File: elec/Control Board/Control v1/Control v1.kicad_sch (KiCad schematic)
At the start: 2 parts, among them J1 Conn_02x12_Odd_Even

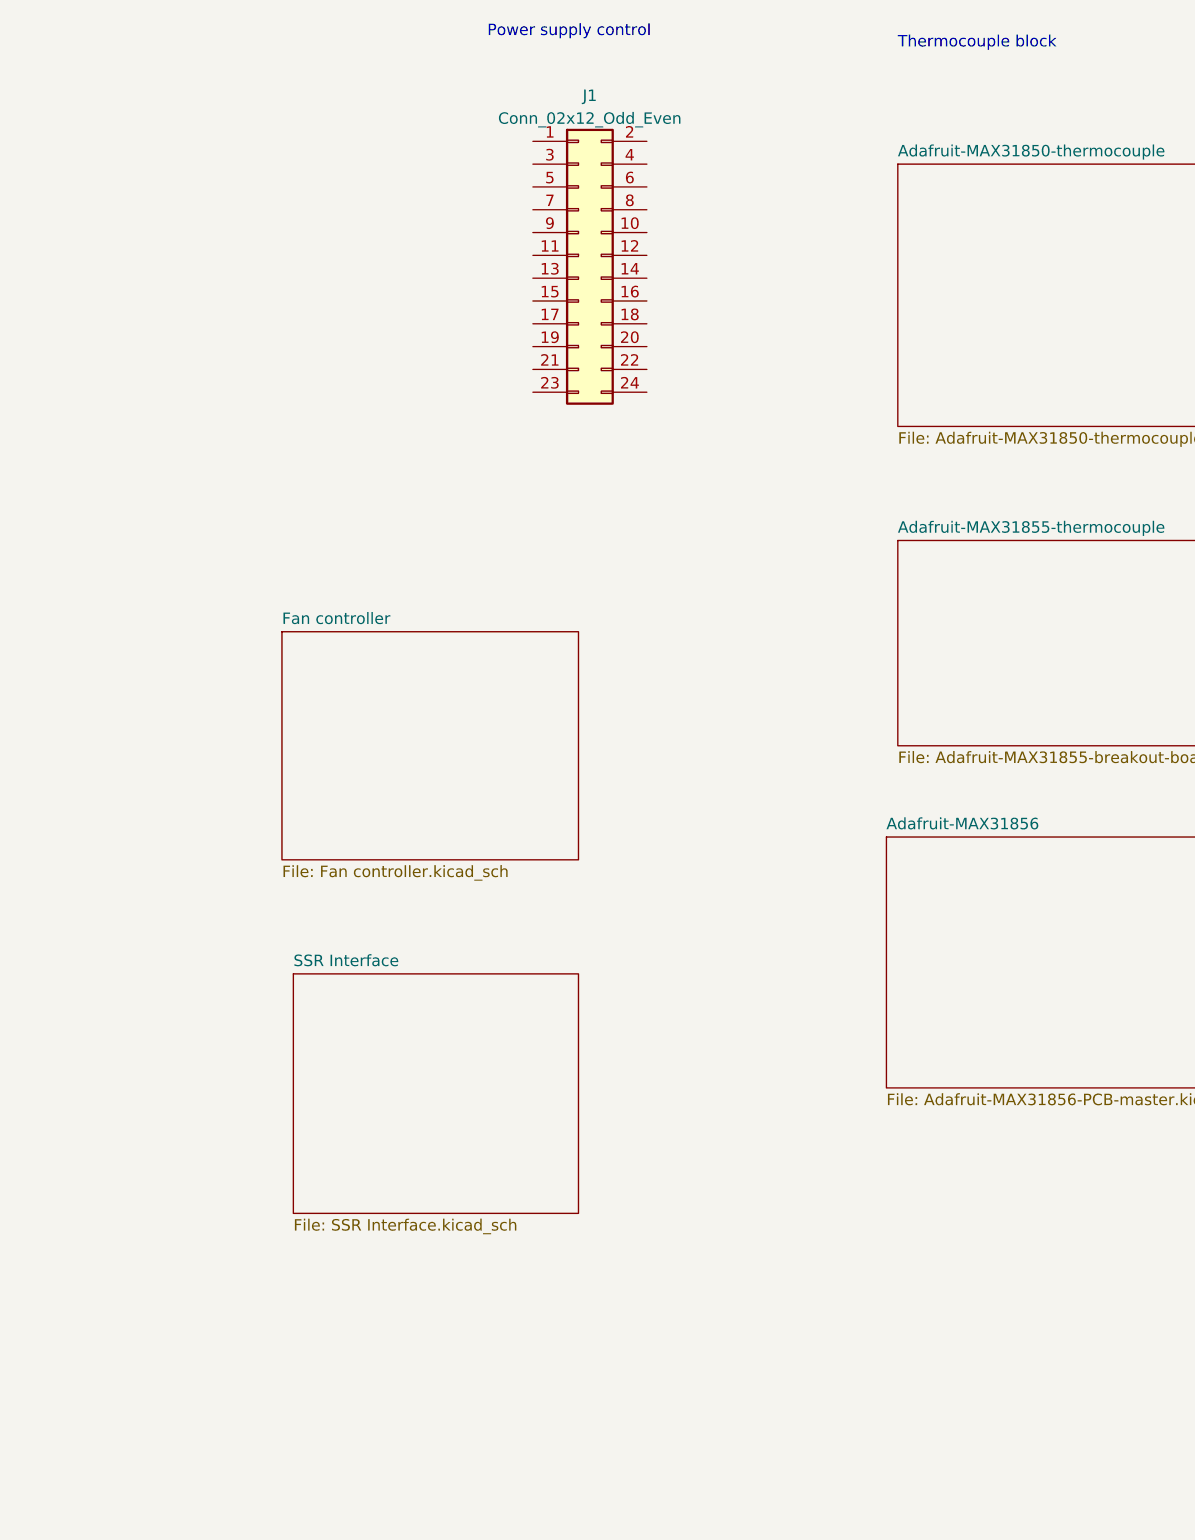
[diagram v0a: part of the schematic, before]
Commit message: added labels for heiarchy sheets, and first pass on basic control interface circuits
Signed-off-by: lokimetasmith <lokimail@gmail.com>
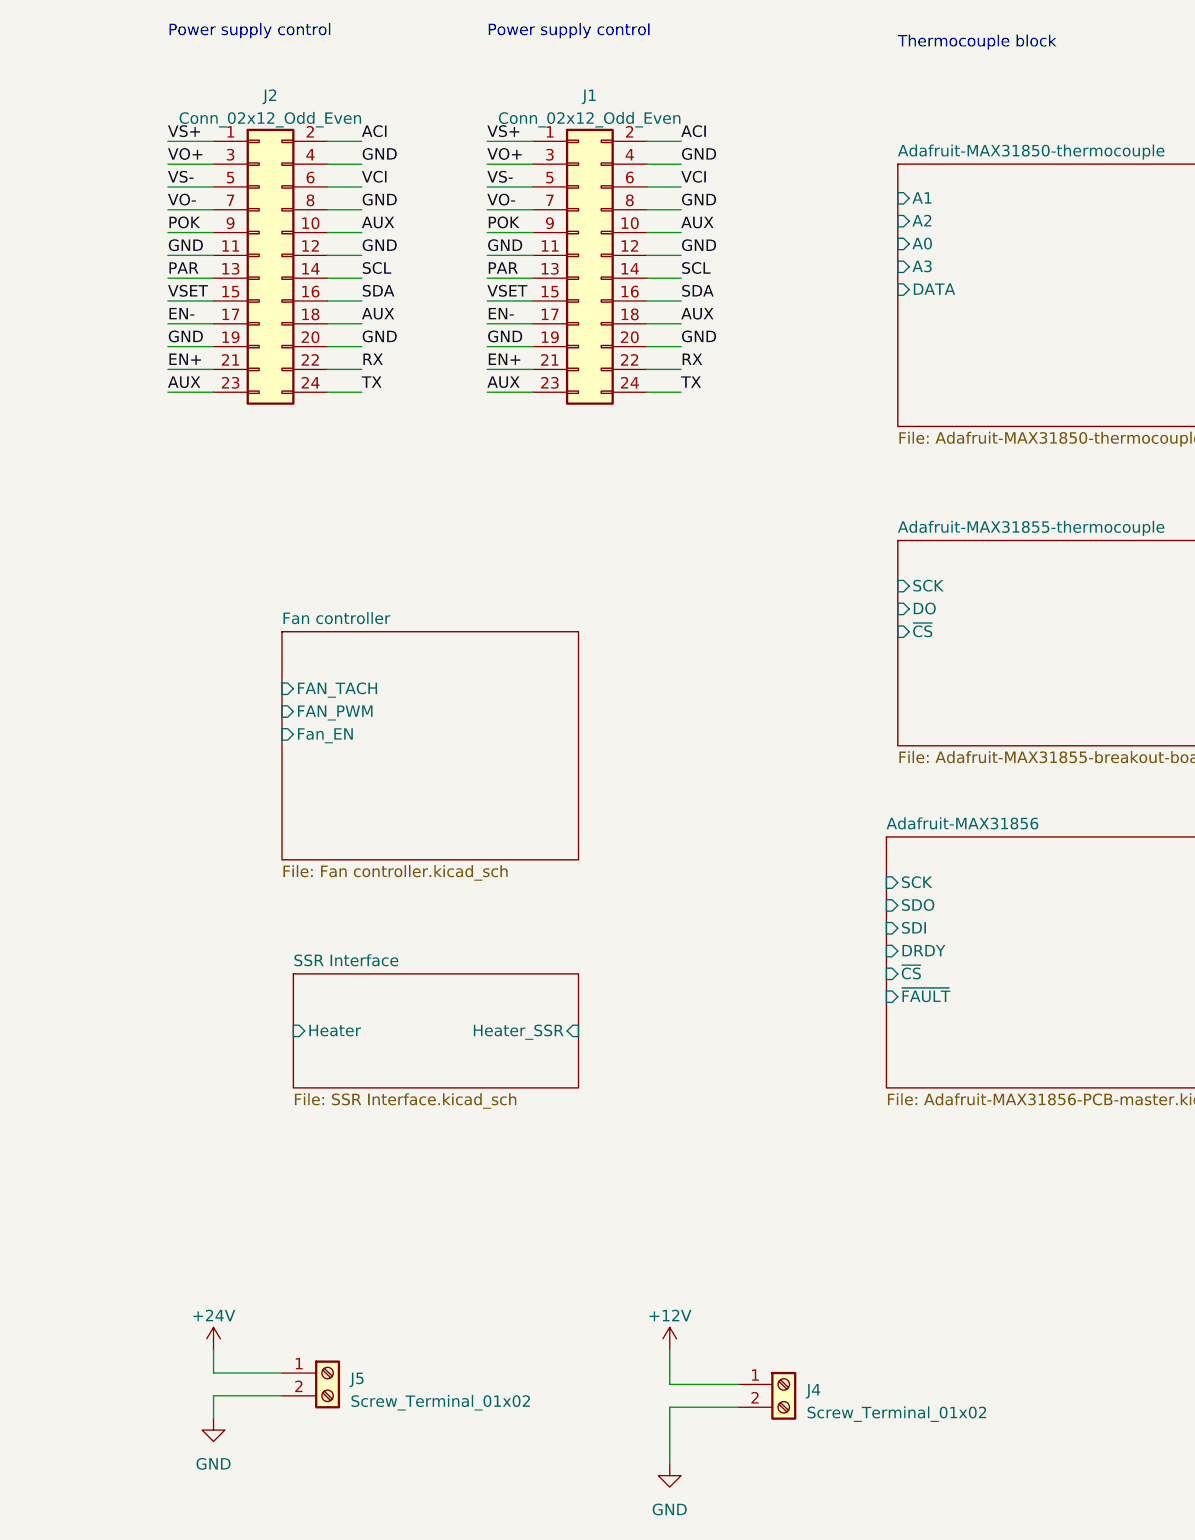
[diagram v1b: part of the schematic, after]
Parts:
- added J2: Conn_02x12_Odd_Even, Connector_PinHeader_2.00mm:PinHeader_2x12_P2.00mm_Vertical, symbol Connector_Generic:Conn_02x12_Odd_Even
- added J4, J5: Screw_Terminal_01x02, symbol Connector:Screw_Terminal_01x02
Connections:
- net VS+: now reaches J1.1 (Pin_1)
- net VS+: now also J2.1 (Pin_1)
- net AUX: now reaches J1.10 (Pin_10)
- net AUX: now also J1.18 (Pin_18), J1.23 (Pin_23), J2.10 (Pin_10), J2.18 (Pin_18), J2.23 (Pin_23)
- net GND: now reaches J1.11 (Pin_11)
- net GND: now also J1.12 (Pin_12), J1.19 (Pin_19), J1.20 (Pin_20), J1.4 (Pin_4), J1.8 (Pin_8), J2.11 (Pin_11), J2.12 (Pin_12), J2.19 (Pin_19), J2.20 (Pin_20), J2.4 (Pin_4), J2.8 (Pin_8), J4.2 (Pin_2), J5.2 (Pin_2)
- net PAR: now reaches J1.13 (Pin_13)
- net PAR: now also J2.13 (Pin_13)
- net SCL: now reaches J1.14 (Pin_14)
- net SCL: now also J2.14 (Pin_14)
- net VSET: now reaches J1.15 (Pin_15)
- net VSET: now also J2.15 (Pin_15)
- net SDA: now reaches J1.16 (Pin_16)
- net SDA: now also J2.16 (Pin_16)
- net EN-: now reaches J1.17 (Pin_17)
- net EN-: now also J2.17 (Pin_17)
- net ACI: now reaches J1.2 (Pin_2)
- net ACI: now also J2.2 (Pin_2)
- net EN+: now reaches J1.21 (Pin_21)
- net EN+: now also J2.21 (Pin_21)
- net RX: now reaches J1.22 (Pin_22)
- net RX: now also J2.22 (Pin_22)
- net TX: now reaches J1.24 (Pin_24)
- net TX: now also J2.24 (Pin_24)
- net VO+: now reaches J1.3 (Pin_3)
- net VO+: now also J2.3 (Pin_3)
- net VS-: now reaches J1.5 (Pin_5)
- net VS-: now also J2.5 (Pin_5)
- net VCI: now reaches J1.6 (Pin_6)
- net VCI: now also J2.6 (Pin_6)
- net VO-: now reaches J1.7 (Pin_7)
- net VO-: now also J2.7 (Pin_7)
- net POK: now reaches J1.9 (Pin_9)
- net POK: now also J2.9 (Pin_9)
- new net +12V: J4.1 (Pin_1)
- new net +24V: J5.1 (Pin_1)
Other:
- sheet Adafruit-MAX31850-thermocouple ports: added A0, A1, A2, A3, DATA; removed none
- sheet Adafruit-MAX31855-thermocouple ports: added DO, SCK, ~{CS}; removed none
- sheet Adafruit-MAX31856 ports: added DRDY, SCK, SDI, SDO, ~{CS}, ~{FAULT}; removed none
- sheet Fan controller ports: added FAN_PWM, FAN_TACH, Fan_EN; removed none
- sheet SSR Interface ports: added Heater, Heater_SSR; removed none

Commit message: imported Lee's changed inputs into the folder Control Board,
Also added in Robert's pin labels

ToDo: clean up broken links, and import in the layout files from Lee's project

Clean up the fan control pinout, the DB25 is a bit of a mess
consider using IDC to DB25 connectors for ease of assembly and installation.


Signed-off-by: lokimetasmith <lokimail@gmail.com>
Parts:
- removed J2: Conn_02x12_Odd_Even, Connector_PinHeader_2.00mm:PinHeader_2x12_P2.00mm_Vertical, symbol Connector_Generic:Conn_02x12_Odd_Even
- added H1, H2, H3, H4, H5: MountingHole_Pad_3.5mm, GeneralPurposeAlarmDevicePCB:MountingHole_3.5mm_Pad_Via, symbol GPAD_SCH_LIB:MountingHole_Pad_3.5mm
- added J14, J15, J17, J18: Conn_01x08, Connector_PinSocket_2.54mm:PinSocket_1x08_P2.54mm_Vertical, symbol Connector_Generic:Conn_01x08
- added J16: Conn_01x08, Connector_PinHeader_2.54mm:PinHeader_1x08_P2.54mm_Vertical, symbol Connector_Generic:Conn_01x08
- added J19: Conn_02x18_Odd_Even, Connector_PinSocket_2.54mm:PinSocket_2x18_P2.54mm_Vertical, symbol Connector_Generic:Conn_02x18_Odd_Even
- added J20: Conn_01x10_MountingPin, Connector_PinSocket_2.54mm:PinSocket_1x10_P2.54mm_Vertical, symbol Connector_Generic_MountingPin:Conn_01x10_MountingPin
- added J7: DB9_Female_MountingHoles, Connector_Dsub:DSUB-9_Female_Horizontal_P2.77x2.84mm_EdgePinOffset4.94mm_Housed_MountingHolesOffset7.48mm, symbol Connector:DB9_Female_MountingHoles
- added MF1: PCB_PolyVent_SPI_Controller_VER1, NA, symbol GPAD_SCH_LIB:PCB_GPAD_VER1
- added SW1: SW_DIP_x08, PubInv_PCB:SMDIP-16_L11.39_W6.7mm, symbol Switch:SW_DIP_x08
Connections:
- net RX is gone; now on net AUX: J1.22 (Pin_22)
- net TX is gone; now on net D_PSU_TX: J1.24 (Pin_24)
- net ACI: now also J1.14 (Pin_14); no longer J1.2 (Pin_2)
- net AUX: now also J1.11 (Pin_11); no longer J1.10 (Pin_10), J1.23 (Pin_23)
- net EN+: now also J1.12 (Pin_12); no longer J1.21 (Pin_21)
- net EN-: now also J1.10 (Pin_10); no longer J1.17 (Pin_17)
- net GND: now also A1.GND1 (GND), A1.GND2 (GND), A1.GND3 (GND), A1.GND5 (GND), A1.GND6 (GND), J1.13 (Pin_13), J1.15 (Pin_15), J1.17 (Pin_17), J1.21 (Pin_21), J1.5 (Pin_5), J1.9 (Pin_9), H1.1, H2.1, H3.1, H4.1, H5.1, J16.2 (Pin_2), J16.3 (Pin_3), J19.35 (Pin_35), J19.36 (Pin_36), J20.4 (Pin_4), J7.0 (PAD), J7.3, J7.6, J7.7, J7.8, J7.9; no longer J1.11 (Pin_11), J1.12 (Pin_12), J1.19 (Pin_19), J1.20 (Pin_20), J1.4 (Pin_4), J1.8 (Pin_8)
- net PAR: now also J1.8 (Pin_8); no longer J1.13 (Pin_13)
- net POK: now also J1.6 (Pin_6); no longer J1.9 (Pin_9)
- net SCL: now also A1.D21 (D21/SCL), J1.20 (Pin_20); no longer J1.14 (Pin_14)
- net SDA: now also A1.D20 (D20/SDA), J1.19 (Pin_19); no longer J1.16 (Pin_16)
- net VCI: now also J1.16 (Pin_16); no longer J1.6 (Pin_6)
- net VO+: now also J1.1 (Pin_1); no longer J1.3 (Pin_3)
- net VO-: now also J1.3 (Pin_3); no longer J1.7 (Pin_7)
- net VS+: now also J1.2 (Pin_2); no longer J1.1 (Pin_1)
- net VS-: now also J1.4 (Pin_4); no longer J1.5 (Pin_5)
- net VSET: now also J1.7 (Pin_7); no longer J1.15 (Pin_15)
- net +3.3V: now reaches A1.3V3 (3.3V)
- net +3.3V: now also J16.5 (Pin_5)
- net +5V: now reaches A1.5V1 (5V)
- net +5V: now also J16.4 (Pin_4)
- net 5V3: now reaches A1.5V3 (5V)
- net 5V3: now also J19.1 (Pin_1)
- net 5V4: now reaches A1.5V4 (5V)
- net 5V4: now also J19.2 (Pin_2)
- net BLOWER_TACH: now reaches A1.A0
- net BLOWER_TACH: now also J17.1 (Pin_1)
- net at A1.A1: now also J17.2 (Pin_2)
- net at A1.A10: now also J15.3 (Pin_3)
- net at A1.A11: now also J15.4 (Pin_4)
- net at A1.A2: now also J17.3 (Pin_3)
- net at A1.A3: now also J17.4 (Pin_4)
- net at A1.A4: now also J17.5 (Pin_5)
- net at A1.A5: now also J17.6 (Pin_6)
- net at A1.A6: now also J17.7 (Pin_7)
- net at A1.A7: now also J17.8 (Pin_8)
- net at A1.A8: now also J15.1 (Pin_1)
- net at A1.A9: now also J15.2 (Pin_2)
- net AREF: now reaches A1.AREF
- net AREF: now also J20.3 (Pin_3)
- net CANR: now reaches A1.CANR (CANRX)
- net CANR: now also J15.7 (Pin_7)
- net CANT: now reaches A1.CANT (CANTX)
- net CANT: now also J15.8 (Pin_8)
- net D0: now reaches A1.D0 (D0/RX0)
- net D0: now also J18.1 (Pin_1)
- net D1: now reaches A1.D1 (D1/TX0)
- net D1: now also J18.2 (Pin_2)
- net at A1.D10 (D10_CS0): now also J20.8 (Pin_8)
- net at A1.D11: now also J20.7 (Pin_7)
- net at A1.D12: now also J20.6 (Pin_6)
- net at A1.D13: now also J20.5 (Pin_5)
- net at A1.D14 (D14/TX3): now also J14.1 (Pin_1)
- net at A1.D15 (D15/RX3): now also J14.2 (Pin_2)
- net at A1.D16 (D16/TX2): now also J14.3 (Pin_3)
- net at A1.D17 (D17/RX2): now also J14.4 (Pin_4)
- net D_PSU_TX: now reaches A1.D18 (D18/TX1)
- net D_PSU_TX: now also J14.5 (Pin_5)
- net D_PSU_RX: now reaches A1.D19 (D19/RX1)
- net D_PSU_RX: now also J1.23 (Pin_23), J14.6 (Pin_6)
- net at A1.D2: now also J18.3 (Pin_3)
- net at A1.D22: now also J19.3 (Pin_3)
- net D23: now reaches A1.D23
- net D23: now also J14.7 (Pin_7), J19.4 (Pin_4)
- net at A1.D24: now also J19.5 (Pin_5)
- net D25: now reaches A1.D25
- net D25: now also J19.6 (Pin_6)
- net at A1.D26: now also J19.7 (Pin_7)
- net D27: now reaches A1.D27
- net D27: now also J19.8 (Pin_8)
- net at A1.D28: now also J19.9 (Pin_9)
- net D29: now reaches A1.D29
- net D29: now also J19.10 (Pin_10)
- net at A1.D3: now also J18.4 (Pin_4)
- net at A1.D30: now also J19.11 (Pin_11)
- net D31: now reaches A1.D31
- net D31: now also J19.12 (Pin_12)
- net at A1.D32: now also J19.13 (Pin_13)
- net D33: now reaches A1.D33
- net D33: now also J19.14 (Pin_14)
- net at A1.D34: now also J19.15 (Pin_15)
- net D35: now reaches A1.D35
- net D35: now also J19.16 (Pin_16)
- net at A1.D36: now also J19.17 (Pin_17)
- net D37: now reaches A1.D37
- net D37: now also J19.18 (Pin_18)
- net at A1.D38: now also J19.19 (Pin_19)
- net D39: now reaches A1.D39
- net D39: now also J19.20 (Pin_20)
- net ONE_WIRE_TC: now reaches A1.D4 (D4_CS1)
- net ONE_WIRE_TC: now also J18.5 (Pin_5)
- net at A1.D40: now also J19.21 (Pin_21)
- net D41: now reaches A1.D41
- net D41: now also J19.22 (Pin_22)
- net at A1.D42: now also J19.23 (Pin_23)
- net D43: now reaches A1.D43
- net D43: now also J19.24 (Pin_24)
- net at A1.D44: now also J19.25 (Pin_25)
- net D45: now reaches A1.D45
- net D45: now also J19.26 (Pin_26)
- net at A1.D46: now also J19.27 (Pin_27)
- net D47: now reaches A1.D47
- net D47: now also J19.28 (Pin_28)
- net at A1.D48: now also J19.29 (Pin_29)
- net D49: now reaches A1.D49
- net D49: now also J19.30 (Pin_30)
- net at A1.D5: now also J18.6 (Pin_6)
- net at A1.D50: now also J19.31 (Pin_31)
- net D51: now reaches A1.D51
- net D51: now also J19.32 (Pin_32)
- net at A1.D52 (D52_CS2): now also J19.33 (Pin_33)
- net at A1.D53: now also J19.34 (Pin_34)
- net at A1.D6: now also J18.7 (Pin_7)
- net at A1.D7: now also J18.8 (Pin_8)
- net at A1.D8: now also J20.10 (Pin_10)
- net BLOWER_PWM: now reaches A1.D9
- net BLOWER_PWM: now also J20.9 (Pin_9)
- net DAC0: now reaches A1.DAC0
- net DAC0: now also J15.5 (Pin_5)
- net DAC1: now reaches A1.DAC1
- net DAC1: now also J15.6 (Pin_6)
- net at A1.IORF (IOREF): now also J16.7 (Pin_7)
- net CIPO: now reaches A1.MISO (SPI_MISO)
- net COPI: now reaches A1.MOSI (SPI_MOSI)
- net at A1.RST1 (RESET): now also J16.6 (Pin_6)
- net SPI_SCK: now reaches A1.SCK (SPI_SCK)
- net SCL1: now reaches A1.SCL1
- net SCL1: now also J20.1 (Pin_1)
- net SDA1: now reaches A1.SDA1
- net SDA1: now also J20.2 (Pin_2)
- net at A1.VIN: now also J16.1 (Pin_1)
- new net D22: J14.8 (Pin_8)
- new net I2C_LevelShift/SCL_5V: J7.2
- new net I2C_LevelShift/SDA_5V: J7.4
- new net SPI_ControllerLevel_Shifter/COPI_nCS: SW1.1, SW1.2, SW1.3, SW1.4, SW1.5, SW1.6, SW1.7, SW1.8
- new net nCS1_3V3: SW1.16
- new net nCS2_3V3: SW1.15
- new net nCS3_3V3: SW1.14
- new net nCS4_3V3: SW1.13
- new net nCS5_3V3: SW1.12
- new net nCS6_3V3: SW1.11
- new net nCS7_3V3: SW1.10
- new net nCS8_3V3: SW1.9
- no-connect marks 0 -> 1
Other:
- added sheet I2C_LevelShift (I2C_Level_Shifter.kicad_sch)
- added sheet SPI_ControllerLevel_Shifter (SPI_ControllerLevel_Shifter.kicad_sch)
- note added: "Due Pin Number Connection Notes A0 Blower Tachometer D4 Dallas One-Wire connection to Thermocouple Breakouts D9 Blower PWM D18 Digital Power Supply TF800 Pin 23 This is Serial1 TX https://assets.alliedelec.com/v1560852133/Datasheets/1d230174086e96b6e4801d1c963649f3.pdf D19 Digital Power Supply TF800 Pin 24 This is Serial1 RX https://assets.alliedelec.com/v1560852133/Datasheets/1d230174086e96b6e48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"
- note added: "| **Pin #** | **Function** | **Description** | **Pin #** | **Function** | **Description** | |----------- |-------------- |-------------------------------------- |----------- |-------------- |-------------------------------------- | | 1 | VS+ | Remote Sense (+) | 13 | ACI | I Program | | 2 | VO+ | Positive Output Voltage | 14 | GND | Ground | | 3 | VX- | Remote Sense (-) | 15 | VCI | V Program | |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"
- moved on the sheet: A1, J1, J4, J5

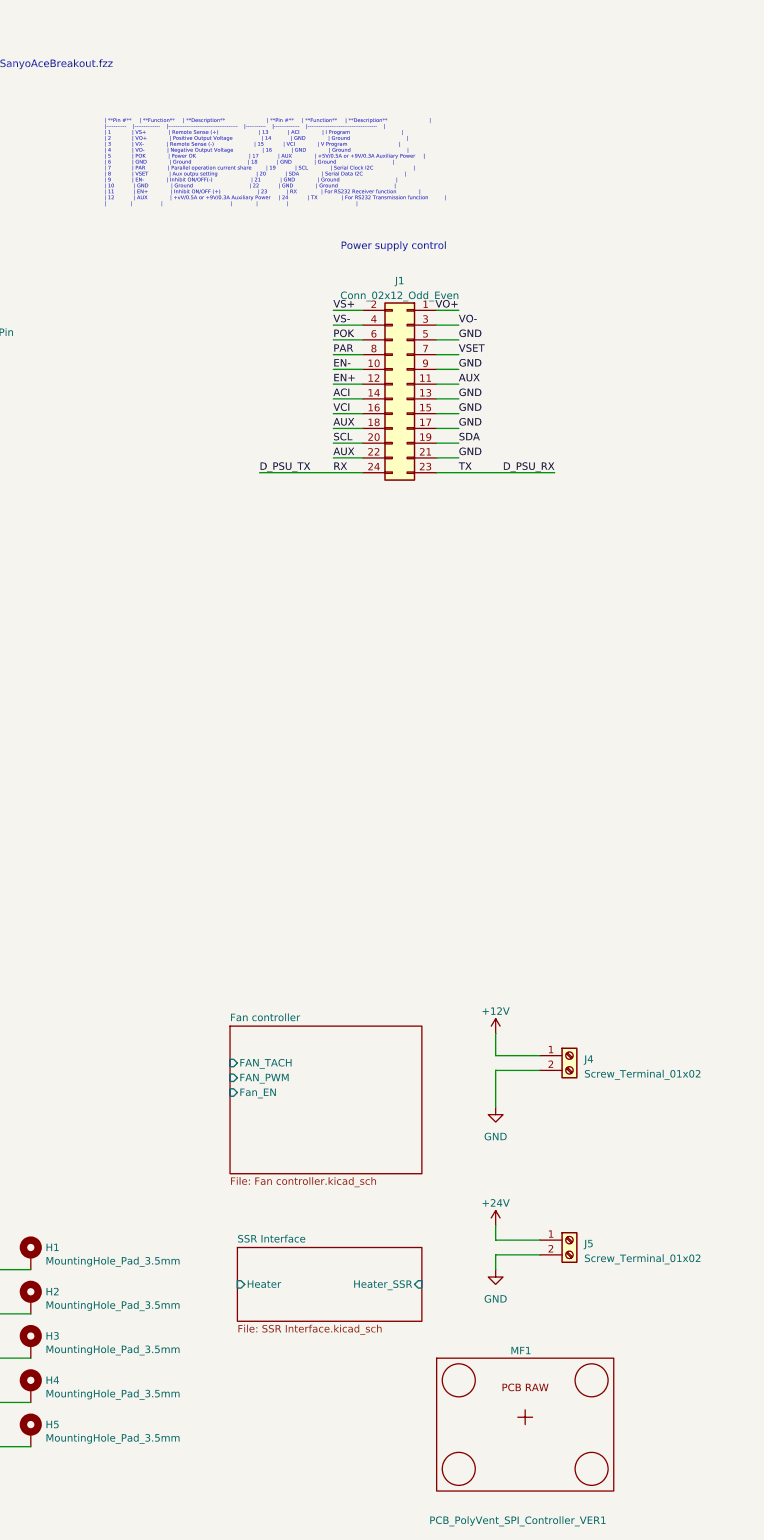
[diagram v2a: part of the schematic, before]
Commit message: Add Lees PublicInvention submodule library. Update Control V1 project and schematic for new library.
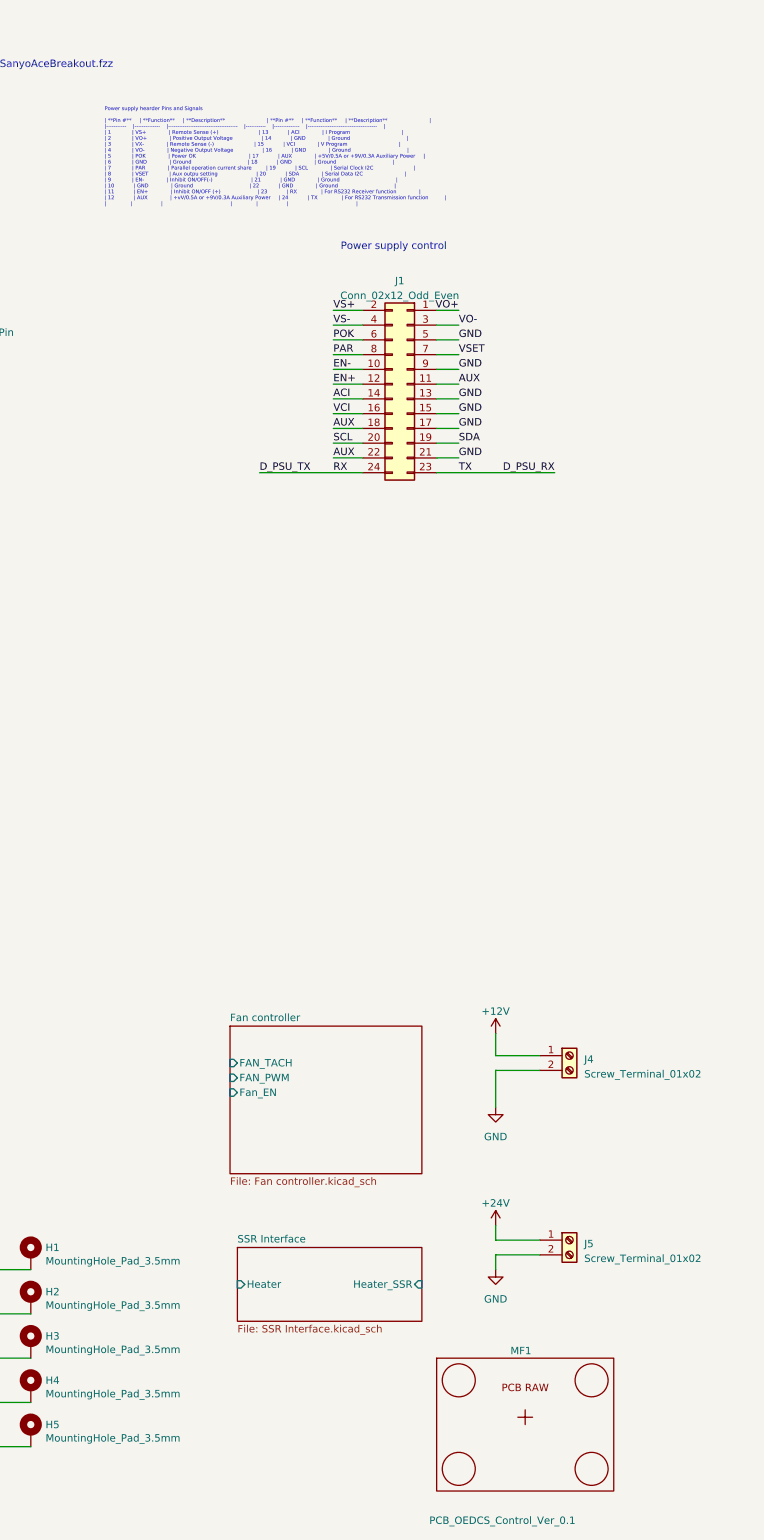
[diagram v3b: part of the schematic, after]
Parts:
- MF1: value PCB_PolyVent_SPI_Controller_VER1 -> PCB_OEDCS_Control_Ver_0.1; Distributor 1 JLCPCB -> PublicInvention; MPN PCB_PolyVent_SPI_Controller_VER1 -> PCB_OEDCS_Control_Ver_0.1
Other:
- note added: "Power supply hearder Pins and Signals | **Pin #** | **Function** | **Description** | **Pin #** | **Function** | **Description** | |----------- |-------------- |-------------------------------------- |----------- |-------------- |-------------------------------------- | | 1 | VS+ | Remote Sense (+) | 13 | ACI | I Program | | 2 | VO+ | Positive Output Voltage | 14 | GND | Ground | | 3 | VX- | Remot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"
- note removed: "| **Pin #** | **Function** | **Description** | **Pin #** | **Function** | **Description** | |----------- |-------------- |-------------------------------------- |----------- |-------------- |-------------------------------------- | | 1 | VS+ | Remote Sense (+) | 13 | ACI | I Program | | 2 | VO+ | Positive Output Voltage | 14 | GND | Ground | | 3 | VX- | Remote Sense (-) | 15 | VCI | V Program | |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"
